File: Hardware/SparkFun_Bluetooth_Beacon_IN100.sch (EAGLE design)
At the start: 24 parts, among them J3 Vertical Qwiic Connector, U1 IN100, Y1 CRYSTAL-26MHZSMD-3.2X2.5

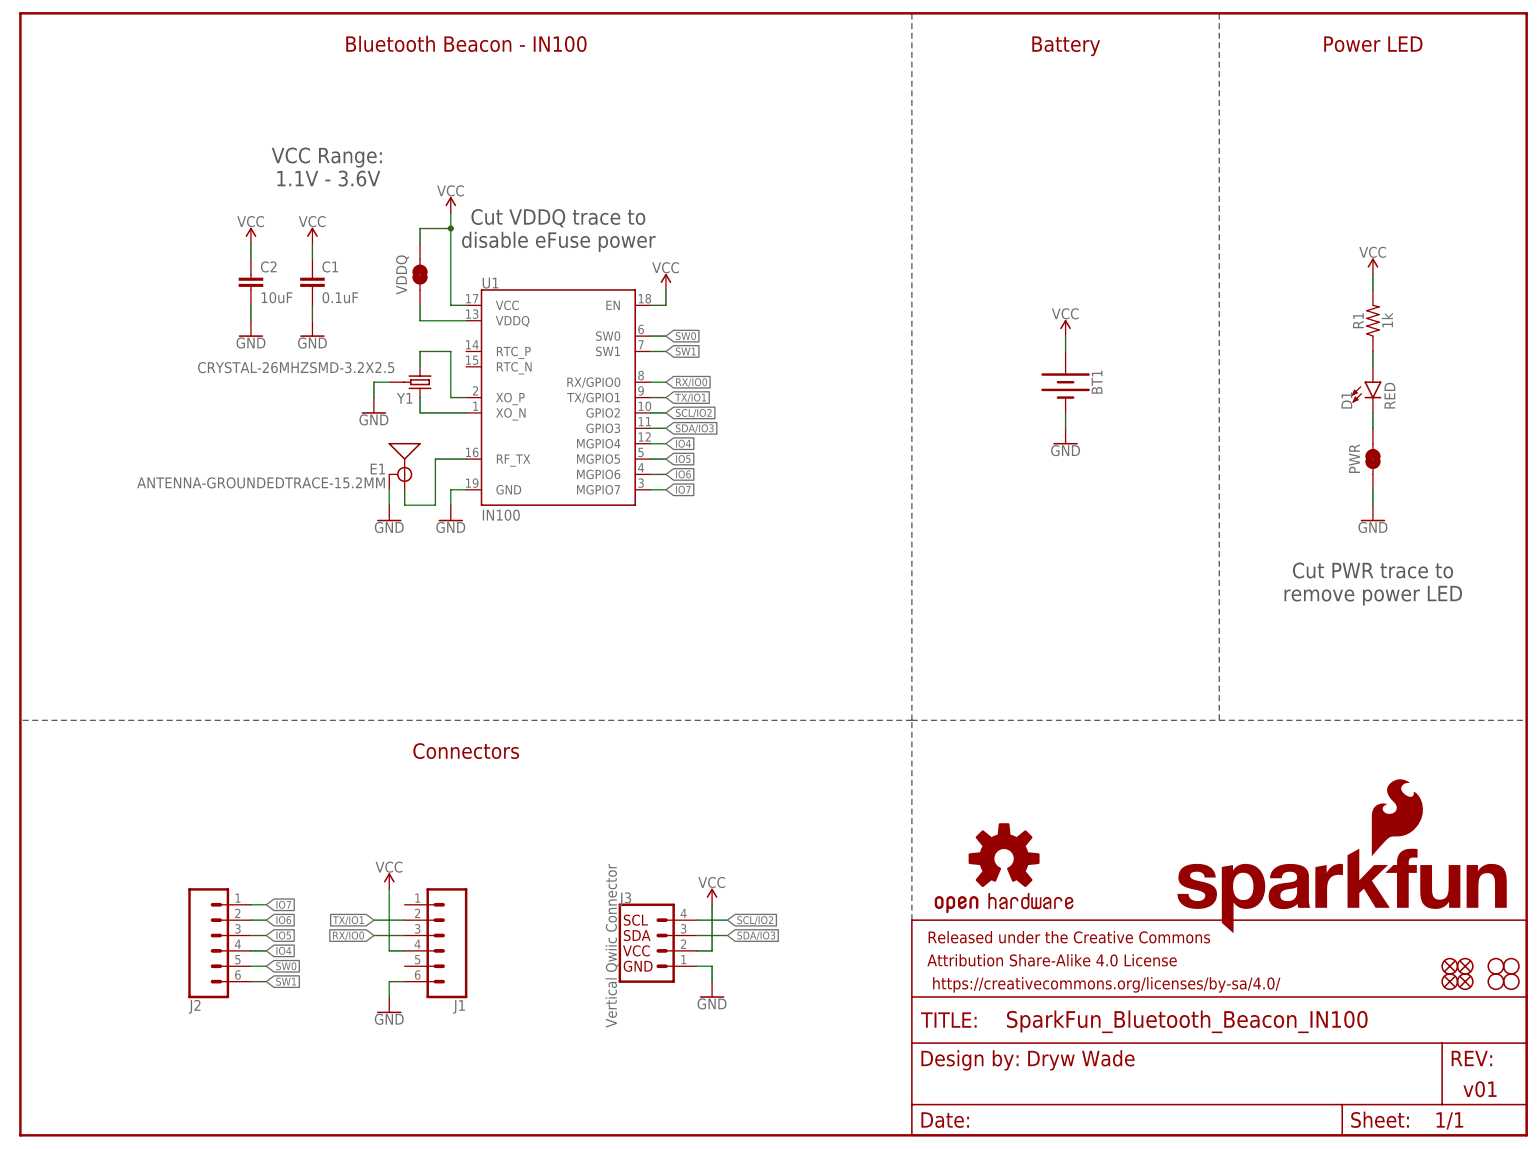
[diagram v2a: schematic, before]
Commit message: Add suggestions from InPlay
Add diodes to isolate VIN from V_BATT
Add RC filter to EN
Add jumper for I2C power selection
Add bulk capacitor to SW0 output
Reroute entire board to accommodate changes
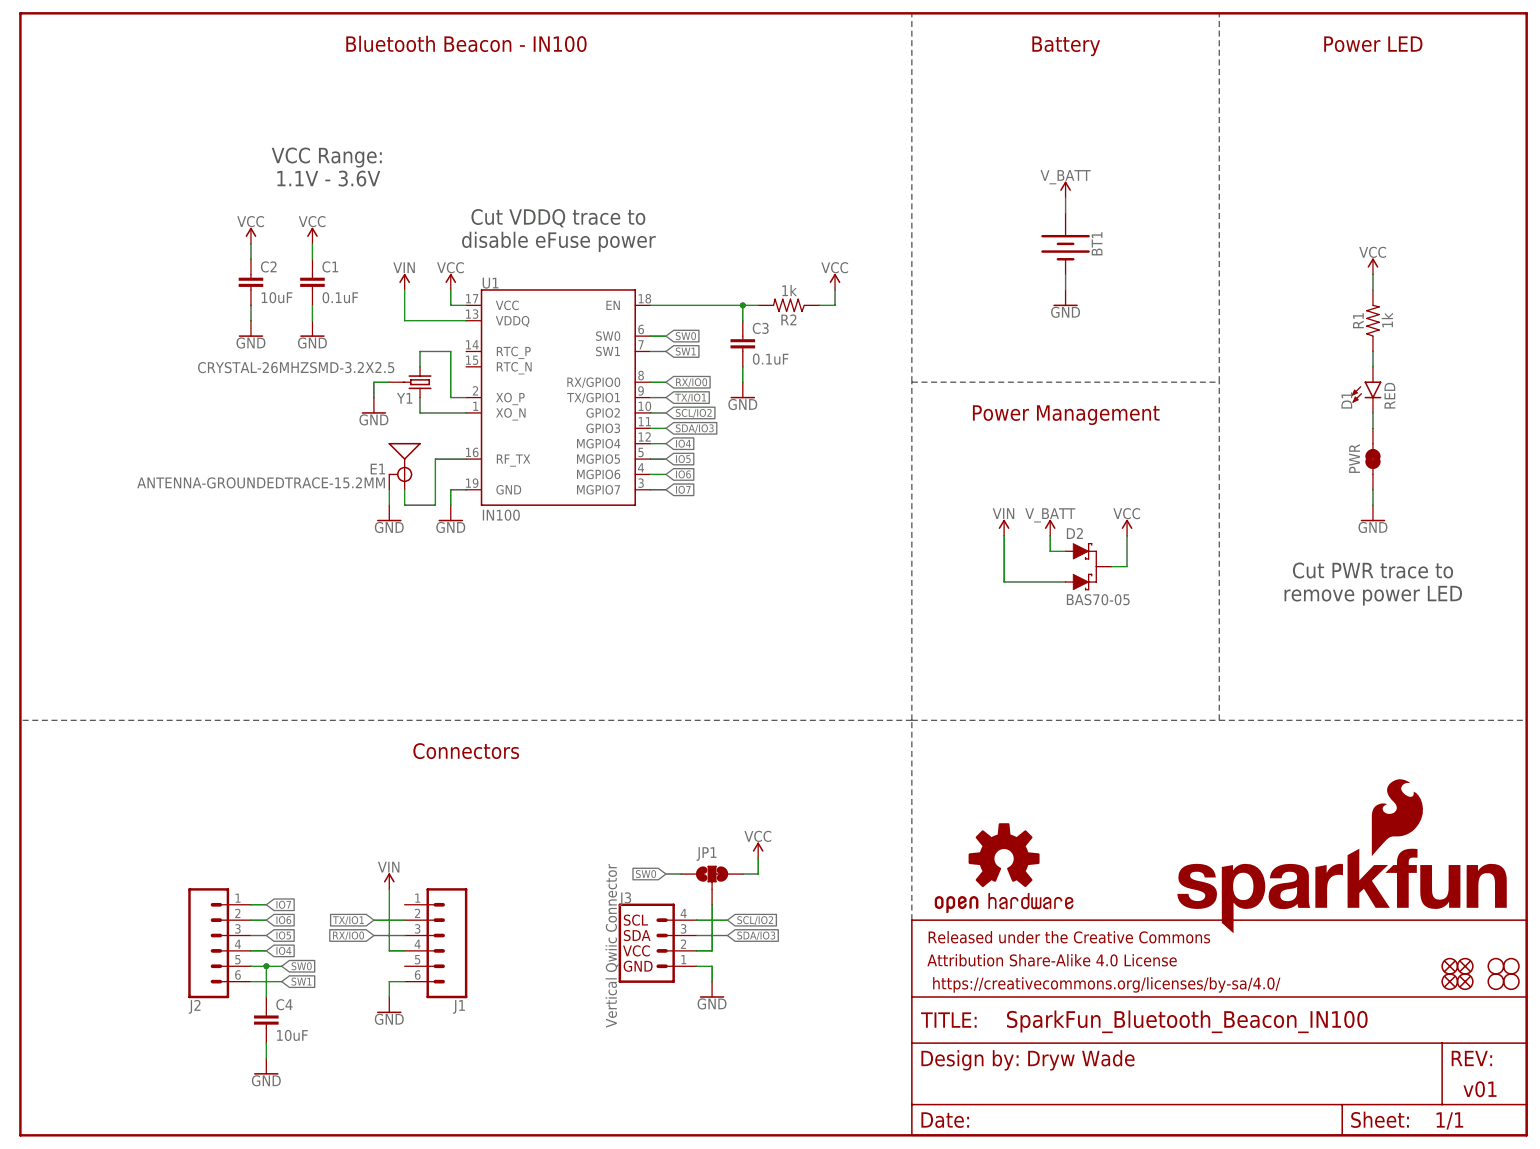
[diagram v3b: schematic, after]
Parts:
- removed VDDQ: JUMPER-SMT_2_NC_TRACE_SILK, SparkFun-Jumpers:JUMPER-SMT_2_NC_TRACE_SILK
- added C3: 0.1uF, SparkFun-Capacitors:0.1UF-0603-25V-(+80/-20%)
- added C4: 10uF, SparkFun-Capacitors:10UF-0603-6.3V-20%
- added D2: BAS70-05, SparkFun-DiscreteSemi:DIODE-SCHOTTKY-DUAL
- added JP1: JUMPER-SMT_3_1-NC_TRACE_SILK, SparkFun-Jumpers:JUMPER-SMT_3_1-NC_TRACE_SILK
- added R2: 1k, SparkFun-Resistors:1KOHM-0603-1/10W-1%
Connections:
- new net N$7: J3.2, JP1.2
- new net VIN: D2.A1, J1.4, U1.VDDQ
- new net V_BATT: BT1.+, D2.A
- net GND: now also C3.2, C4.2
- net N$3: now also C3.1, R2.2, U1.EN; no longer U1.VDDQ, VDDQ.1
- net SW0: now also C4.1, JP1.1
- net VCC: now also D2.C, JP1.3, R2.1; no longer BT1.+, J1.4, J3.2, U1.EN, VDDQ.2
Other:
- note added: "Power Management"
- moved on the sheet: BT1

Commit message: V10 updates
Bump version number to v10
Extend pads of IN100 to get better fillet outside of chip
Change all 0603 components to 0402
Add I2C pullups
Swap jumper for I2C bus power to make SW0 default
Add I2C test points
Reposition and reroute for above changes
Add silk label to power LED
Remove "Serial" silk from bottom
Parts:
- removed JP1: JUMPER-SMT_3_1-NC_TRACE_SILK, SparkFun-Jumpers:JUMPER-SMT_3_1-NC_TRACE_SILK
- added BUS: JUMPER-SMT_3_1-NC_TRACE_SILK, SparkFun-Jumpers:JUMPER-SMT_3_1-NC_TRACE_SILK
- added I2C: JUMPER-SMT_3_2-NC_TRACE_SILK, SparkFun-Jumpers:JUMPER-SMT_3_2-NC_TRACE_SILK
- added R3, R4: 2.2k, SparkFun-Resistors:2.2KOHM-0402T-1/16W-1%
- added TP1, TP2: TEST-POINT3, SparkFun-Connectors:TEST-POINT3
- C1, C3: device SparkFun-Capacitors:0.1UF-0603-25V-(+80/-20%) -> SparkFun-Capacitors:0.1UF-0402T-6.3V-10%-X7R
- C2, C4: device SparkFun-Capacitors:10UF-0603-6.3V-20% -> SparkFun-Capacitors:10UF-0402T-6.3V-20%
- D1: device SparkFun-LED:LED-RED0603 -> SparkFun-LED:LED-RED_0402
- R1: value 1k -> 2.2k; device SparkFun-Resistors:1KOHM-0603-1/10W-1% -> SparkFun-Resistors:2.2KOHM-0402T-1/16W-1%
- R2: device SparkFun-Resistors:1KOHM-0603-1/10W-1% -> SparkFun-Resistors:1KOHM-0402T-1/16W-1%
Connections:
- new net N$8: BUS.2, I2C.2, J3.2
- new net N$9: I2C.3, R3.2
- net N$7: now also I2C.1, R4.2; no longer J3.2, JP1.2
- net SCL/IO2: now also R3.1, TP2.1
- net SDA/IO3: now also R4.1, TP1.1
- net SW0: now also BUS.3; no longer JP1.1
- net VCC: now also BUS.1; no longer JP1.3
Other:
- note added: "Cut BUS trace and solder other side to switch I2C bus power source"
- note added: "Cut I2C traces to remove I2C pullups"
- note added: "Test Points"
- note added: "v10"
- note removed: "Cut VDDQ trace to disable eFuse power"
- note removed: "v01"
- moved on the sheet: C4, D1, J1, J2, J3, PWR, R1

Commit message: Design review updates
Remove power management diodes
Space out I2C test points
Increase VCC and SW0 net widths to 16 mil
Move crystal to avoid interference from VCC trace underneath
Change "Board info" silk to "Notes"
Add measures for coin cell
Add note in schematic to use CR1225 battery
Add warning in schematic and silk to remove battery when powering with VCC
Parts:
- removed D2: BAS70-05, SparkFun-DiscreteSemi:DIODE-SCHOTTKY-DUAL
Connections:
- removed net VIN: D2.A1, J1.4, U1.VDDQ
- removed net V_BATT: BT1.+, D2.A
- net VCC: now also BT1.+, J1.4, U1.VDDQ; no longer D2.C
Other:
- note added: "Use 3V CR1225 batteries only"
- note added: "WARNING\! Remove battery when providing external power (eg. serial breakout)"
- note removed: "Power Management"
- moved on the sheet: BT1, D1, PWR, R1, TP1, TP2

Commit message: v10 updates
Add reset button
Remove SW0 capacitor
Remove top mounting holes
Add solder pads to identify development / production SKUs
Add Qwiic logo
Increase SFE flame silk logo
Nudge Qwiic connector and test points down 25 mils
Move power LED and EN resistor to left side of battery holder
Move VCC trace away from under RF trace
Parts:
- removed C4: 10uF, SparkFun-Capacitors:10UF-0402T-6.3V-20%
- removed H3, H4: STAND-OFF, SparkFun-Hardware:STAND-OFF
- added DEV, PROD: JUMPER-SMT_2_NC_PASTE_NO-SILK, SparkFun-Jumpers:JUMPER-SMT_2_NC_PASTE_NO-SILK
- added LOGO3: QWIIC_LOGO_3MM, SparkFun-Aesthetics:QWIIC_LOGO_3MM
- added RST: MOMENTARY-SWITCH-SPST-SMD-4.6X2.8MM, SparkFun-Switches:MOMENTARY-SWITCH-SPST-SMD-4.6X2.8MM
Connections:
- removed net N$6: D1.A, R1.1
- new net EN: C3.1, R2.2, RST.1, U1.EN
- net GND: now also RST.2; no longer C4.2
- net N$3: now also PWR.2, R1.1; no longer C3.1, R2.2, U1.EN
- net N$5: now also R1.2; no longer PWR.2
- net SW0: no longer C4.1
- net VCC: now also D1.A; no longer R1.2
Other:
- note added: "Reset Button"
- moved on the sheet: D1, PWR, R1, R2

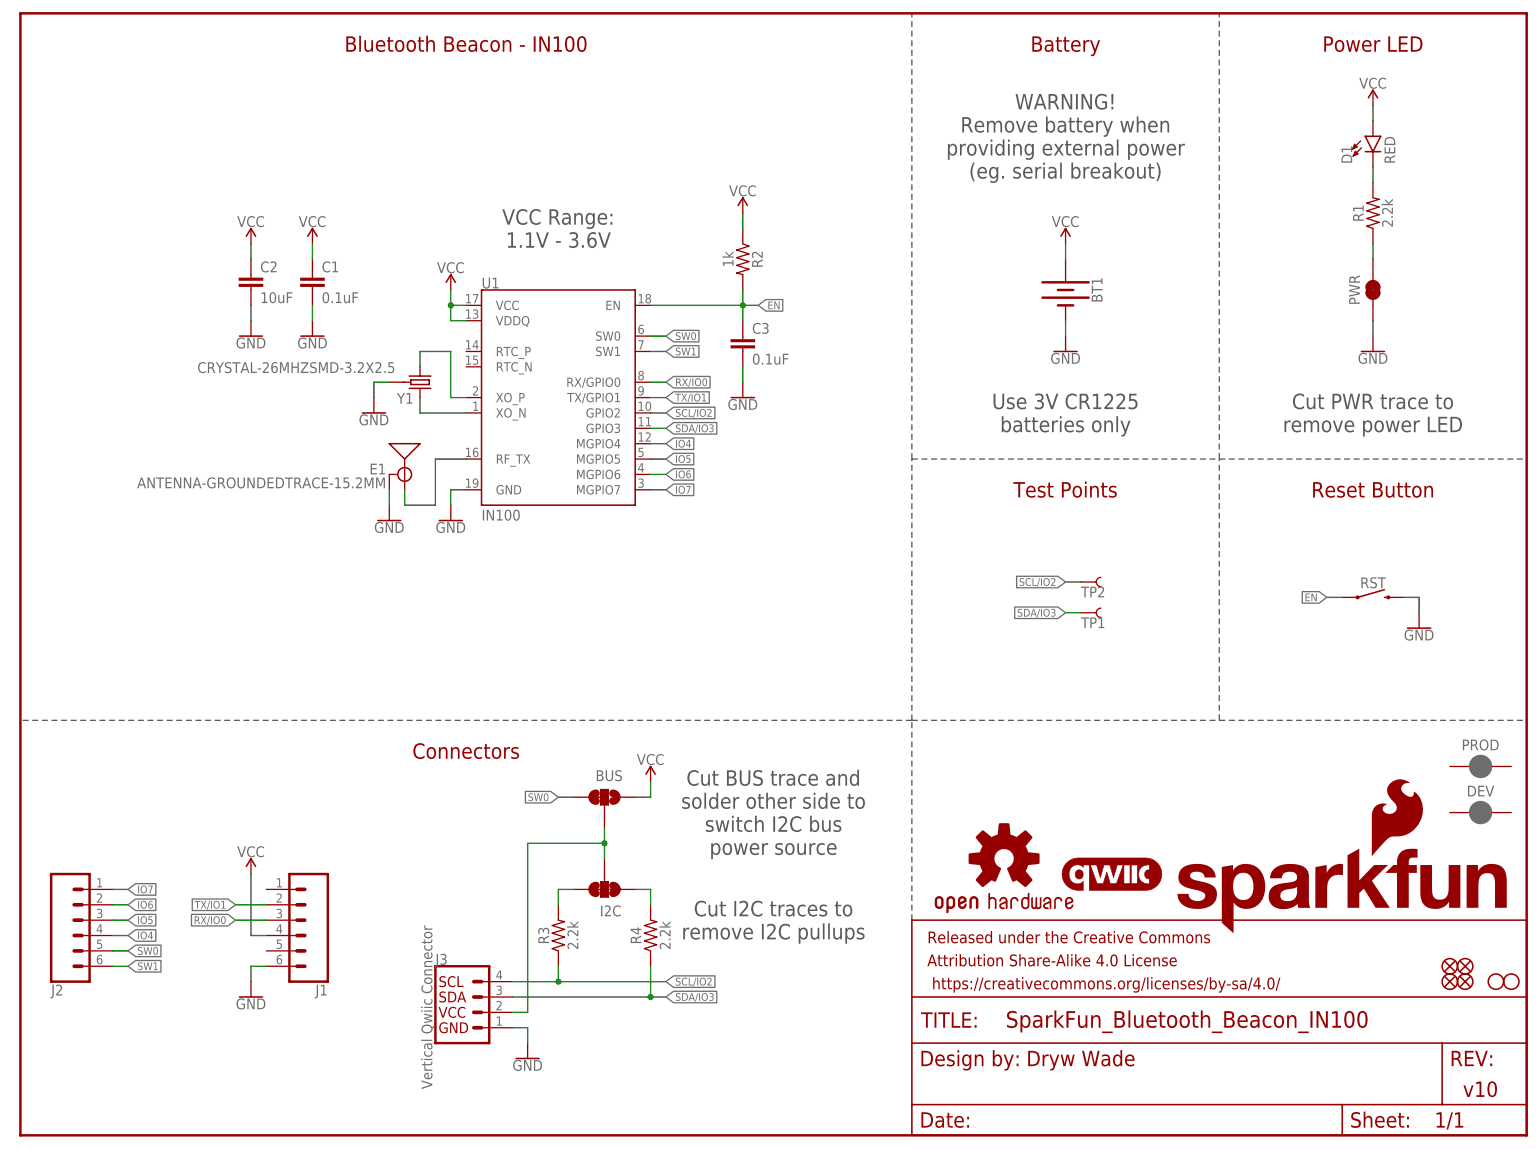
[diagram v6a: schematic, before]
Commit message: Design review updates
Improve GND continuity
Add some small restrict regions to improve copper pour
Nudge "PROD" and "DEV" text away from pads
In schematic, move reset button to near main IC, and replace with Product Identifier pads
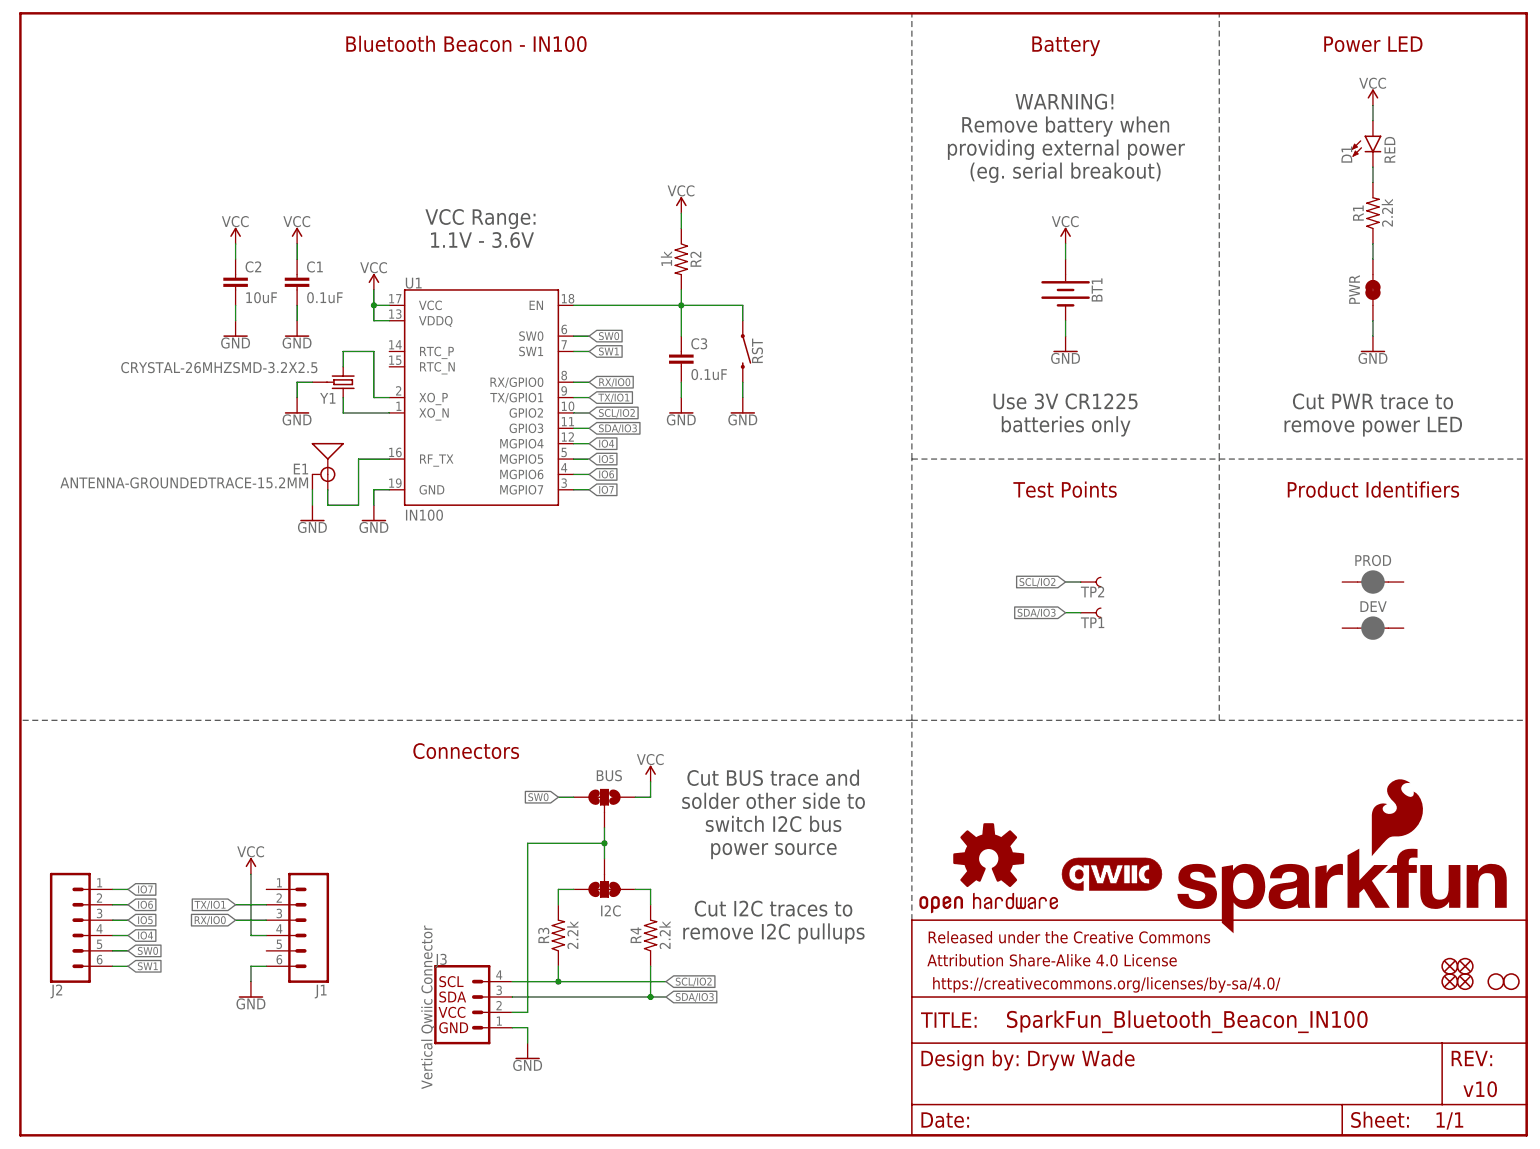
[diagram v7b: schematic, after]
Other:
- note added: "Product Identifiers"
- note removed: "Reset Button"
- moved on the sheet: C1, C2, C3, DEV, E1, PROD, R2, RST, U1, Y1

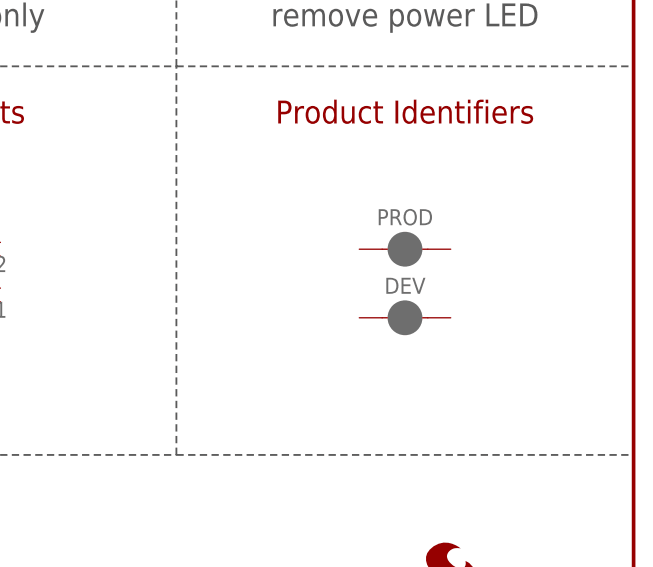
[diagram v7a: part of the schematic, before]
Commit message: Change identifier pads to solid versions
Also approve extraneous DRC jumper overlap error
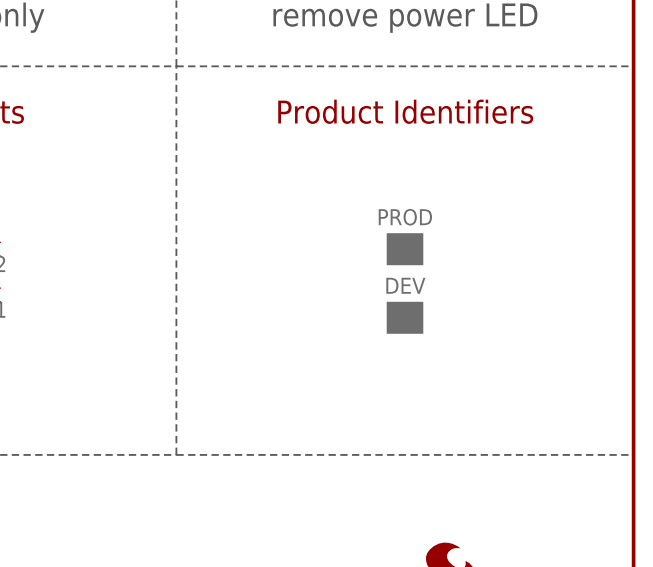
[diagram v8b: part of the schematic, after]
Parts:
- DEV, PROD: value JUMPER-SMT_2_NC_PASTE_NO-SILK -> PROD_ID_PASTE_SILK; device SparkFun-Jumpers:JUMPER-SMT_2_NC_PASTE_NO-SILK -> SparkFun-Aesthetics:PROD_ID_PASTE_SILK
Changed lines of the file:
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@@
 <part name="GND12" library="SparkFun-PowerSymbols" deviceset="GND" device=""/>
 <part name="LOGO3" library="SparkFun-Aesthetics" deviceset="QWIIC_LOGO" device="_3MM"/>
-<part name="PROD" library="SparkFun-Jumpers" deviceset="JUMPER-SMT_2_NC_PASTE" device="_NO-SILK" package3d_urn="urn:adsk.eagle:package:39283/1"/>
-<part name="DEV" library="SparkFun-Jumpers" deviceset="JUMPER-SMT_2_NC_PASTE" device="_NO-SILK" package3d_urn="urn:adsk.eagle:package:39283/1"/>
+<part name="PROD" library="SparkFun-Aesthetics" deviceset="PROD_ID_PASTE" device="_SILK" value="PROD_ID_PASTE_SILK"/>
+<part name="DEV" library="SparkFun-Aesthetics" deviceset="PROD_ID_PASTE" device="_SILK"/>
 </parts>
 <sheets>
